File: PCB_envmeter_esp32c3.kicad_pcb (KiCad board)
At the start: 2 copper layers, 72 x 47.5 mm, 26 parts, among them J1 USB_C_Receptacle_USB2.0_16P, J2 USB_C_Receptacle_Simple, J3 AE-BME680, J4 SSD1306, SW1 Reset, SW2 Mode, U1 ESP32-C3-WROOM-02, U2 AP7333-33SAG, U3 NJM2845DL1-33

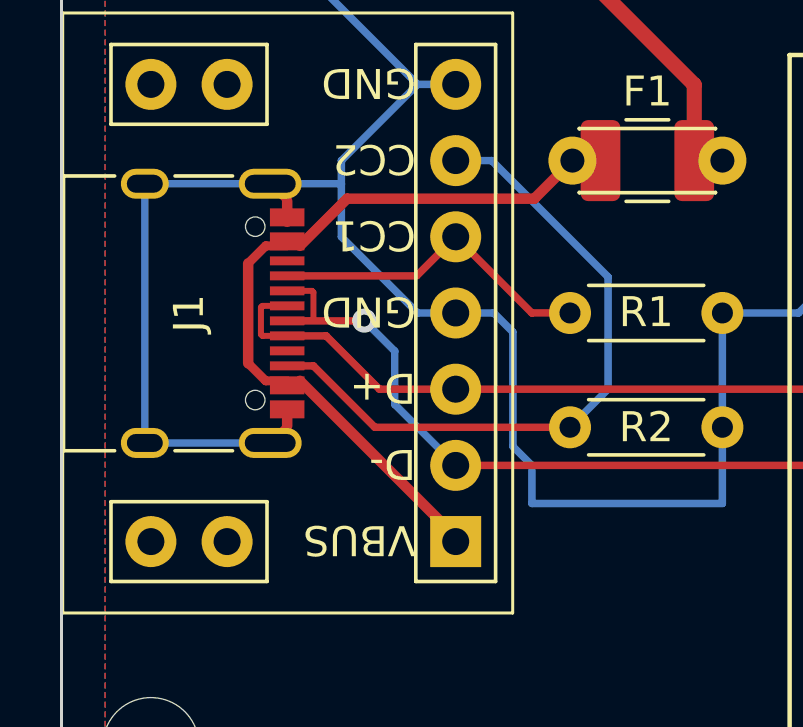
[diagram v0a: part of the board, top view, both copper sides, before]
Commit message: Disconnect shield to GND
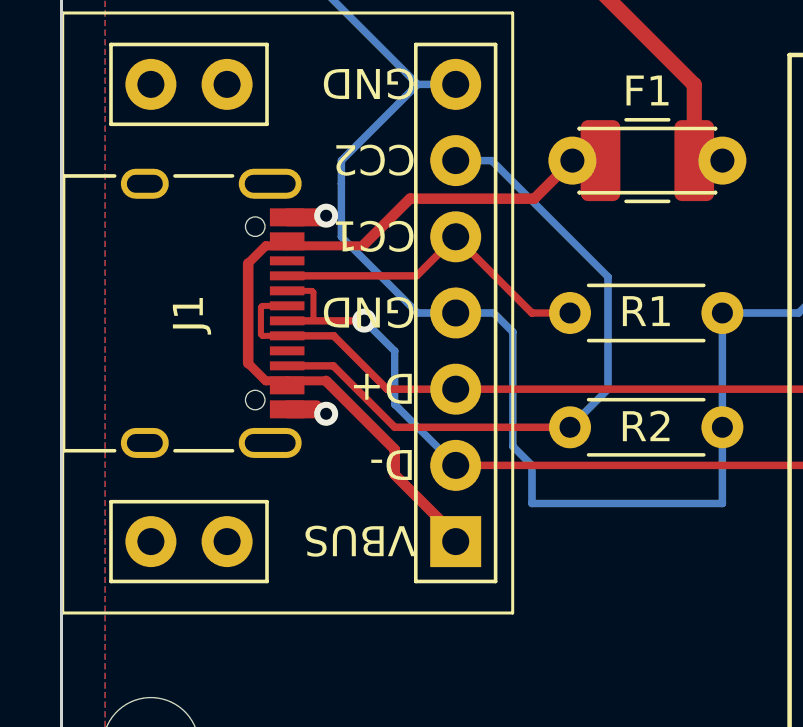
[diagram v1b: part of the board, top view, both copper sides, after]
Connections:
- J1 pad S1: GND -> unconnected-(J1-SHIELD-PadS1)
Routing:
- net GND: track 232.6 -> 215.7 mm, vias 3 -> 5
- net Net-(F1-Pad1): track 25.0 -> 25.7 mm

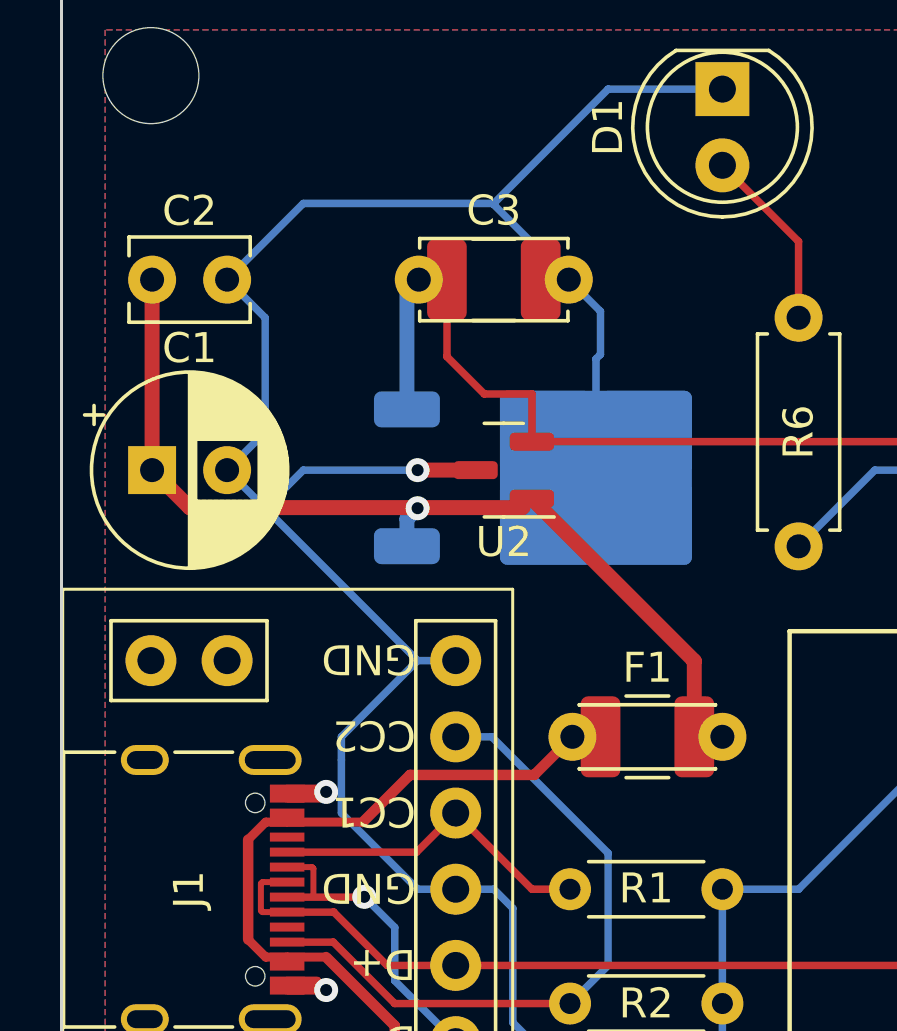
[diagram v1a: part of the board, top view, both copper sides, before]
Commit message: Adjust capacitors position
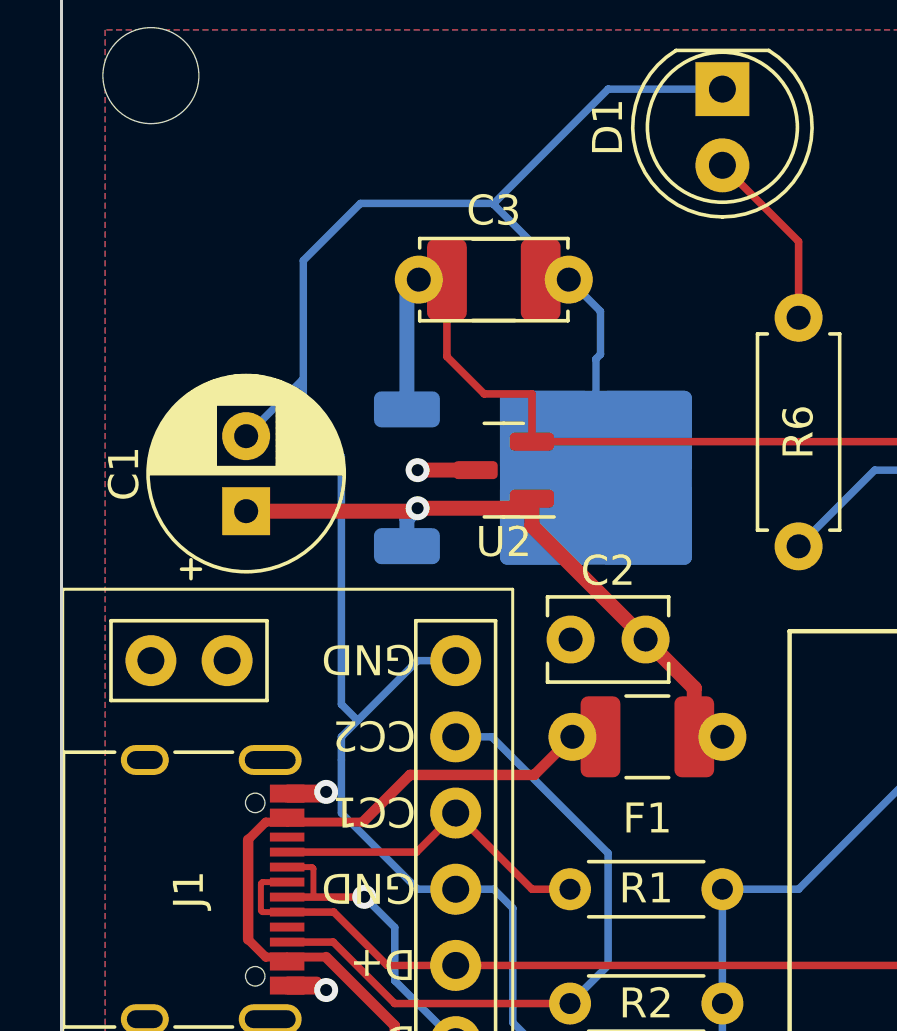
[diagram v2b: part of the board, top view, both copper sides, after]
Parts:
- moved C2 20.4 mm to (54.6, 56.4), turned to 180 degrees
- moved C1 3.42 mm to (41.3, 52.2), turned to 90 degrees
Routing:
- net +5V: track 31.2 -> 21.7 mm
- net GND: track 215.7 -> 209.6 mm

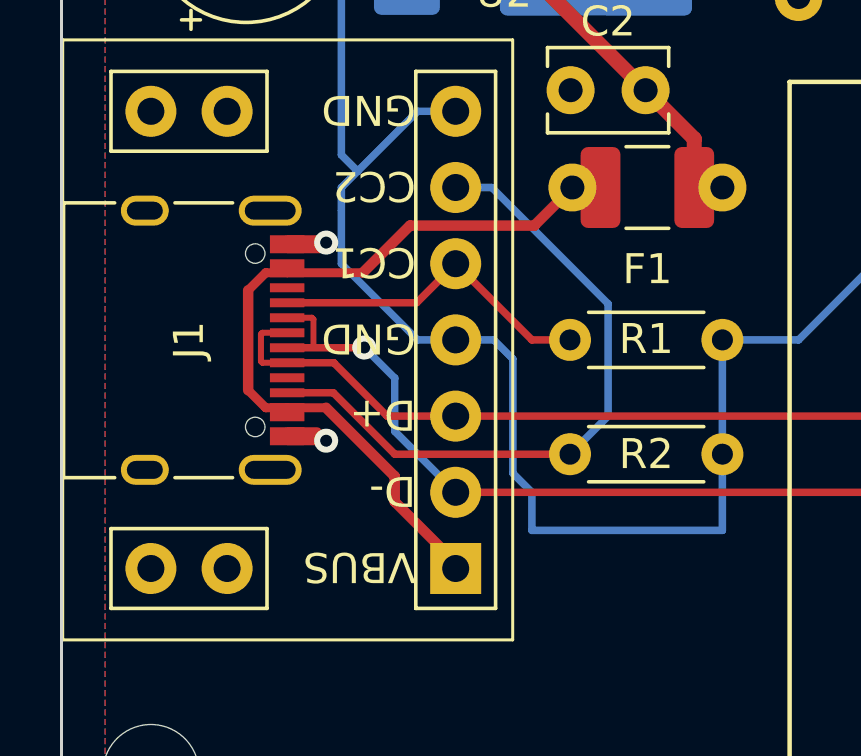
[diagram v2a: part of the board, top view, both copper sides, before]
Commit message: Revise wiring around USB connector
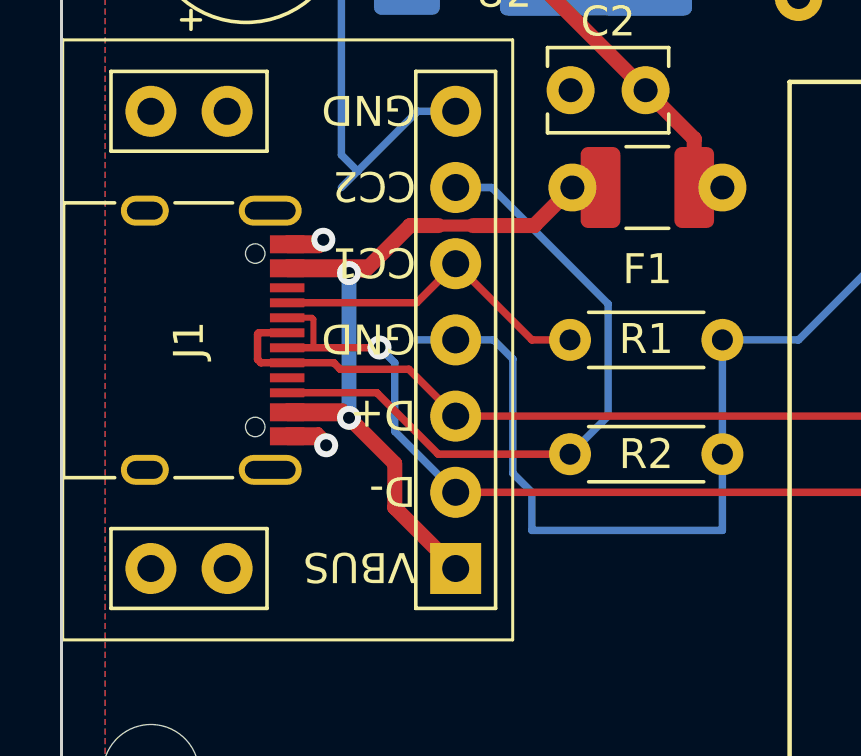
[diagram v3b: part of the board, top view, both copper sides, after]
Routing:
- net GND: track 209.6 -> 203.9 mm
- net Net-(F1-Pad1): track 25.7 -> 29.1 mm, vias 0 -> 2

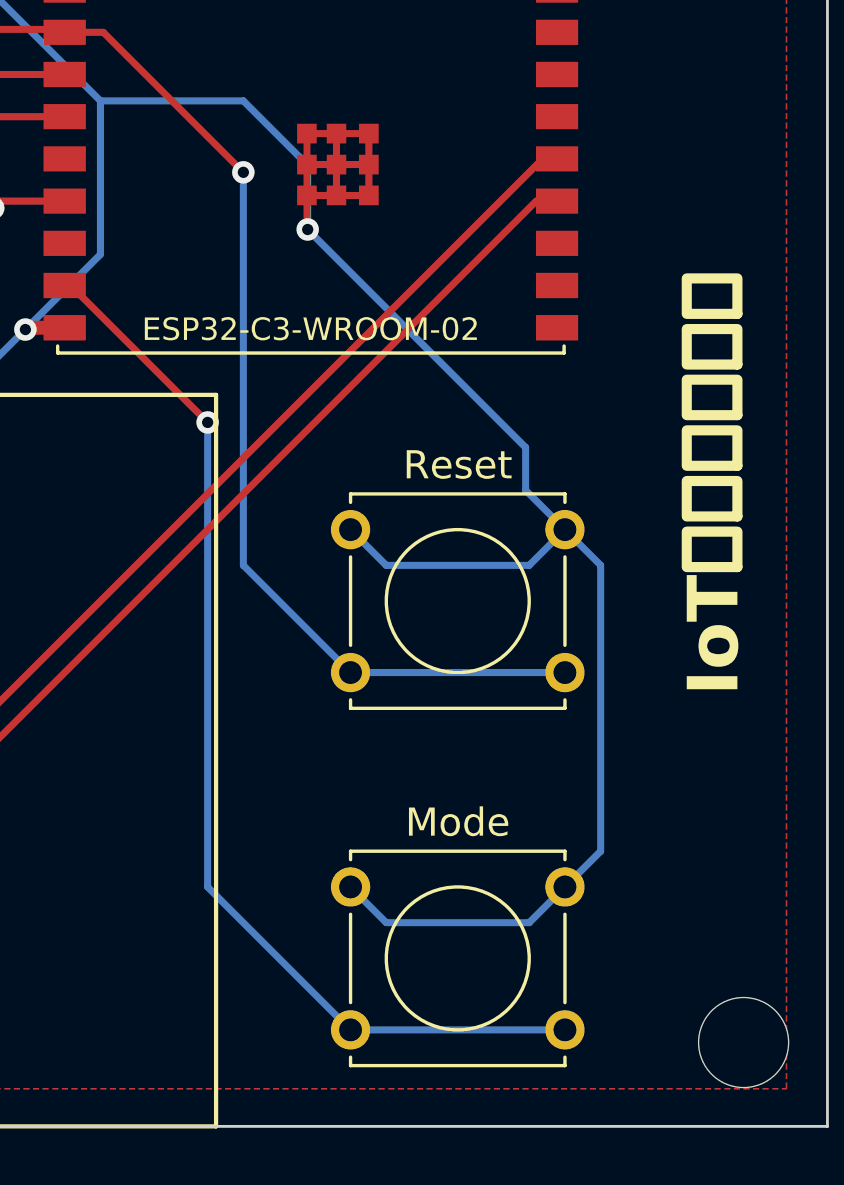
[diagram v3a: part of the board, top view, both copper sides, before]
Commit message: Change footprint of SW1,2
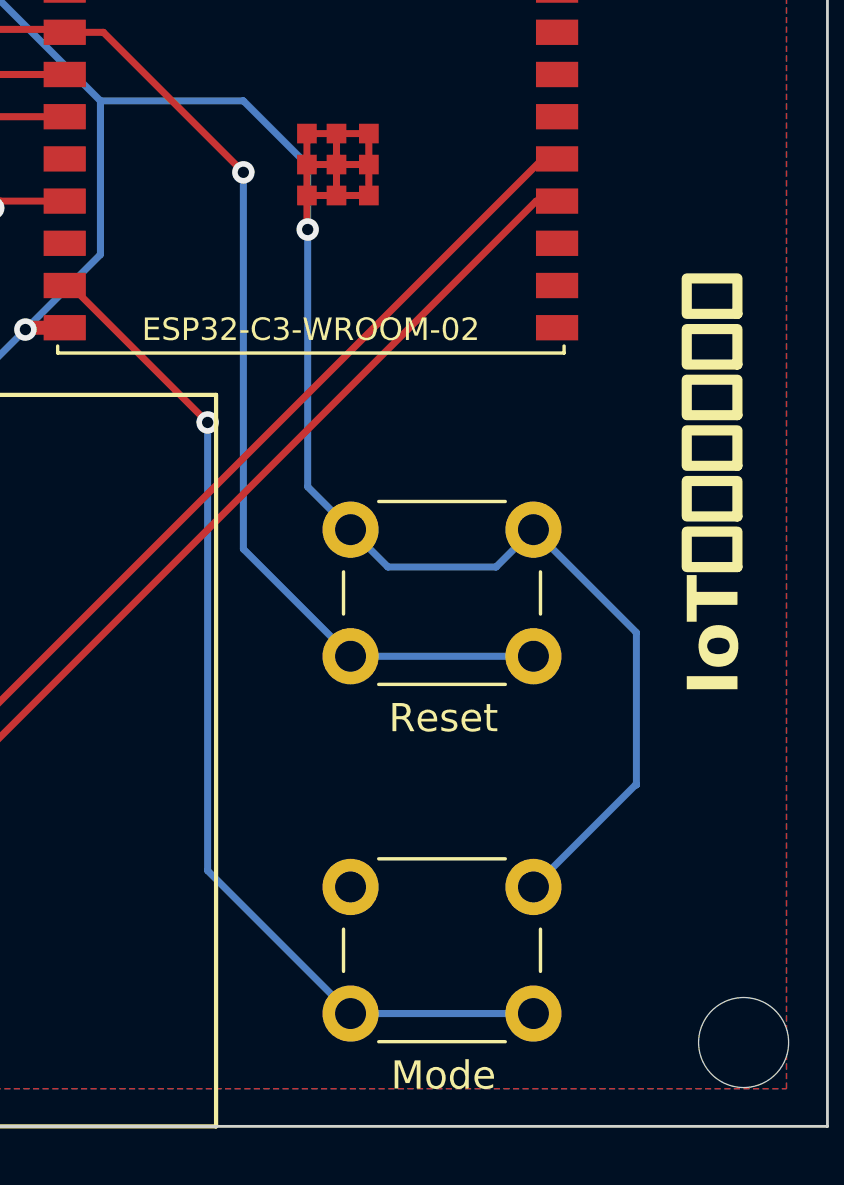
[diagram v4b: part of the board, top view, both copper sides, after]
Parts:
- SW1, SW2: footprint Button_Switch_THT:SW_Tactile_Straight_KSL0Axx1LFTR -> Button_Switch_THT:SW_PUSH_6mm
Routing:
- net GND: track 203.9 -> 193.0 mm
- net Net-(U1-EN/CHIP_PU): track 43.1 -> 41.4 mm
- net Net-(U1-GPIO9): track 38.4 -> 36.7 mm

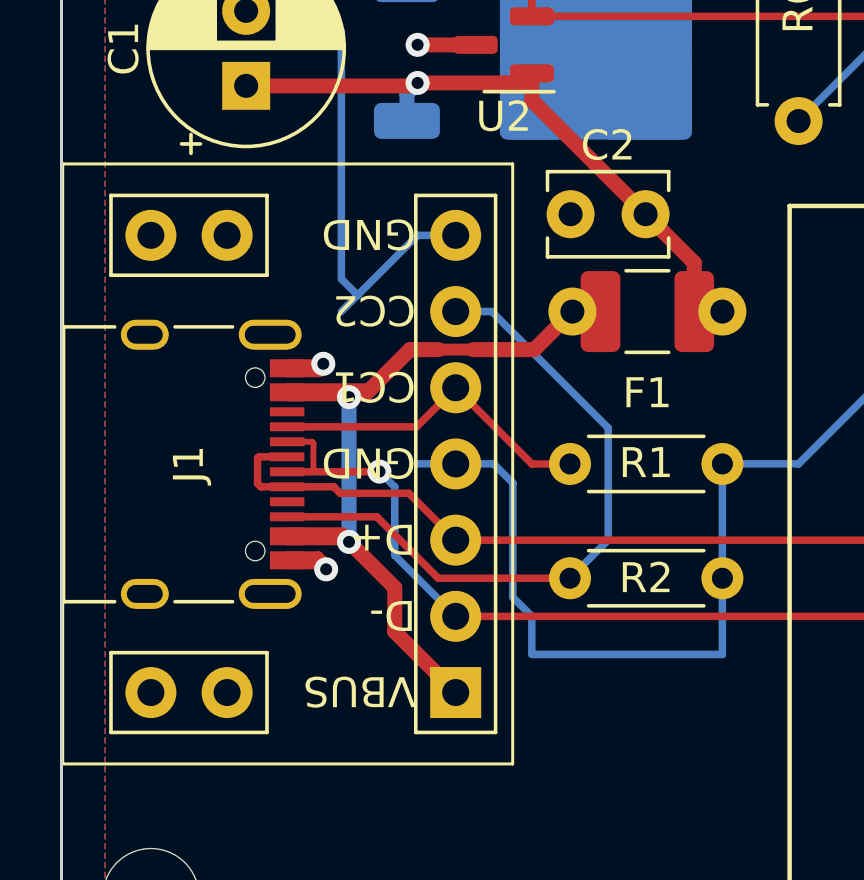
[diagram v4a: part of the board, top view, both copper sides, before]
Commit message: Revise wiring around USB connector
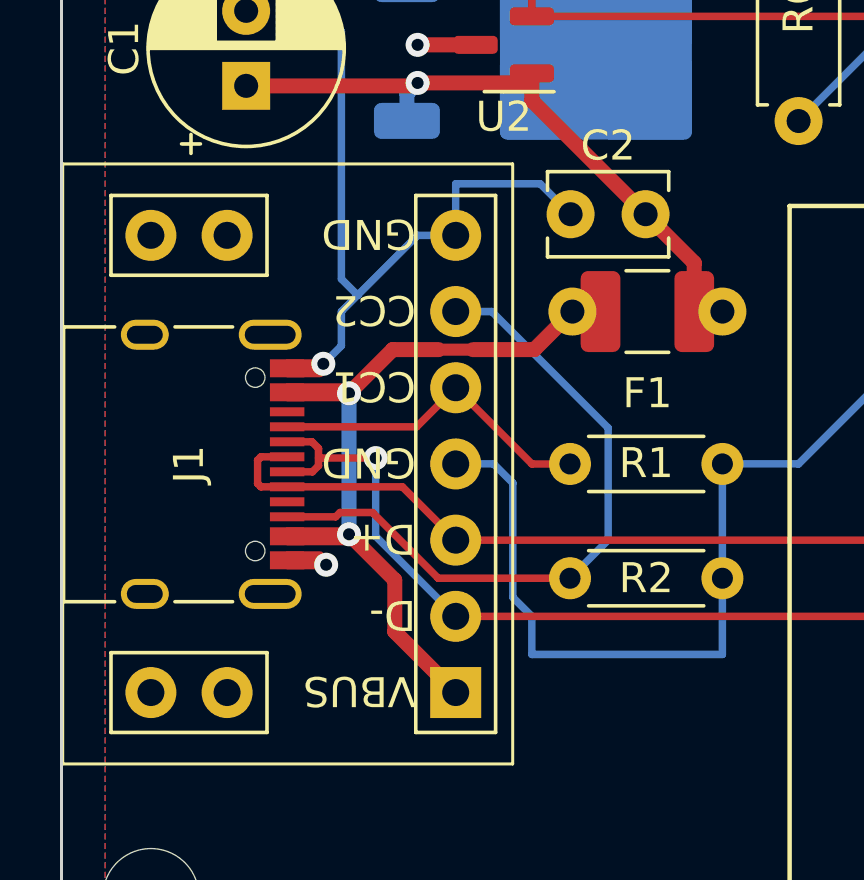
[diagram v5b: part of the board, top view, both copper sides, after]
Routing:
- net GND: track 193.0 -> 198.7 mm
- net Net-(F1-Pad1): track 29.1 -> 28.4 mm

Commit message: Change footprint
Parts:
- removed J2: USB_C_Receptacle_Simple, mylib:Connector_USB_C_simple
- J1: footprint Connector_USB:USB_C_Receptacle_XKB_U262-16XN-4BVC11 -> mylib:Connector_USB_C_simple_combo
- moved J1 12.0 mm to (48.3, 72.4), turned to 180 degrees
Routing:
- net Net-(F1-Pad1): track 28.4 -> 27.8 mm
- net GND: track 198.7 -> 198.1 mm

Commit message: Update F1 footprint
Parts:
- F1: footprint Capacitor_SMD:C_1210_3225Metric_Pad1.33x2.70mm_HandSolder -> Fuse:Fuse_1206_3216Metric_Pad1.42x1.75mm_HandSolder
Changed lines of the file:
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@@
     (pad "" np_thru_hole circle (at 0 0) (size 3.2 3.2) (drill 3.2) (layers "*.Cu" "*.Mask"))
   )
-  (footprint "Capacitor_SMD:C_1210_3225Metric_Pad1.33x2.70mm_HandSolder" (layer "F.Cu")
+  (footprint "Fuse:Fuse_1206_3216Metric_Pad1.42x1.75mm_HandSolder" (layer "F.Cu")
     (at 54.65 59.69)
-    (descr "Capacitor SMD 1210 (3225 Metric), square (rectangular) end terminal, IPC_7351 nominal with elongated pad for handsoldering. (Body size source: IPC-SM-782 page 76, https://www.pcb-3d.com/wordpress/wp-content/uploads/ipc-sm-782a_amendment_1_and_2.pdf), generated with kicad-footprint-generator")
-    (tags "capacitor handsolder")
+    (descr "Fuse SMD 1206 (3216 Metric), square (rectangular) end terminal, IPC_7351 nominal with elongated pad for handsoldering. (Body size source: http://www.tortai-tech.com/upload/download/2011102023233369053.pdf), generated with kicad-footprint-generator")
+    (tags "fuse handsolder")
     (property "Sheetfile" "PCB_envmeter_esp32c3.kicad_sch")
     (property "Sheetname" "")
@@
     (property "ki_keywords" "resettable fuse PTC PPTC polyfuse polyswitch")
     (attr smd)
-    (fp_text reference "F1" (at 0 2.725) (layer "F.SilkS")
+    (fp_text reference "F1" (at 0 2.09) (layer "F.SilkS")
         (effects (font (size 1 1) (thickness 0.15)))
     )
-    (fp_text value "Polyfuse_Small" (at 0 2.3) (layer "F.Fab")
+    (fp_text value "Polyfuse_Small" (at 0 1.82) (layer "F.Fab")
         (effects (font (size 1 1) (thickness 0.15)))
     )
@@
         (effects (font (size 0.8 0.8) (thickness 0.12)))
     )
-    (fp_line (start -0.711252 -1.36) (end 0.711252 -1.36)
+    (fp_line (start -0.602064 -0.91) (end 0.602064 -0.91)
       (stroke (width 0.12) (type solid)) (layer "F.SilkS"))
-    (fp_line (start -0.711252 1.36) (end 0.711252 1.36)
+    (fp_line (start -0.602064 0.91) (end 0.602064 0.91)
       (stroke (width 0.12) (type solid)) (layer "F.SilkS"))
-    (fp_line (start -2.48 -1.6) (end 2.48 -1.6)
+    (fp_line (start -2.45 -1.12) (end 2.45 -1.12)
       (stroke (width 0.05) (type solid)) (layer "F.CrtYd"))
-    (fp_line (start -2.48 1.6) (end -2.48 -1.6)
+    (fp_line (start -2.45 1.12) (end -2.45 -1.12)
       (stroke (width 0.05) (type solid)) (layer "F.CrtYd"))
-    (fp_line (start 2.48 -1.6) (end 2.48 1.6)
+    (fp_line (start 2.45 -1.12) (end 2.45 1.12)
       (stroke (width 0.05) (type solid)) (layer "F.CrtYd"))
-    (fp_line (start 2.48 1.6) (end -2.48 1.6)
+    (fp_line (start 2.45 1.12) (end -2.45 1.12)
       (stroke (width 0.05) (type solid)) (layer "F.CrtYd"))
-    (fp_line (start -1.6 -1.25) (end 1.6 -1.25)
+    (fp_line (start -1.6 -0.8) (end 1.6 -0.8)
       (stroke (width 0.1) (type solid)) (layer "F.Fab"))
-    (fp_line (start -1.6 1.25) (end -1.6 -1.25)
+    (fp_line (start -1.6 0.8) (end -1.6 -0.8)
       (stroke (width 0.1) (type solid)) (layer "F.Fab"))
-    (fp_line (start 1.6 -1.25) (end 1.6 1.25)
+    (fp_line (start 1.6 -0.8) (end 1.6 0.8)
       (stroke (width 0.1) (type solid)) (layer "F.Fab"))
-    (fp_line (start 1.6 1.25) (end -1.6 1.25)
+    (fp_line (start 1.6 0.8) (end -1.6 0.8)
       (stroke (width 0.1) (type solid)) (layer "F.Fab"))
-    (pad "1" smd roundrect (at -1.5625 0) (size 1.325 2.7) (layers "F.Cu" "F.Paste" "F.Mask") (roundrect_rratio 0.1886792453)
+    (pad "1" smd roundrect (at -1.4875 0) (size 1.425 1.75) (layers "F.Cu" "F.Paste" "F.Mask") (roundrect_rratio 0.175439)
       (net 5 "Net-(F1-Pad1)") (pintype "passive"))
-    (pad "2" smd roundrect (at 1.5625 0) (size 1.325 2.7) (layers "F.Cu" "F.Paste" "F.Mask") (roundrect_rratio 0.1886792453)
+    (pad "2" smd roundrect (at 1.4875 0) (size 1.425 1.75) (layers "F.Cu" "F.Paste" "F.Mask") (roundrect_rratio 0.175439)
       (net 1 "+5V") (pintype "passive"))
-    (model "${KICAD6_3DMODEL_DIR}/Capacitor_SMD.3dshapes/C_1210_3225Metric.wrl"
+    (model "${KICAD6_3DMODEL_DIR}/Fuse.3dshapes/Fuse_1206_3216Metric.wrl"
       (offset (xyz 0 0 0))
       (scale (xyz 1 1 1))
